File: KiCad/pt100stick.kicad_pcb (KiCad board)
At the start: 2 copper layers, 15.7 x 20.8 mm, 9 parts, among them U1 MAX31865ATP_

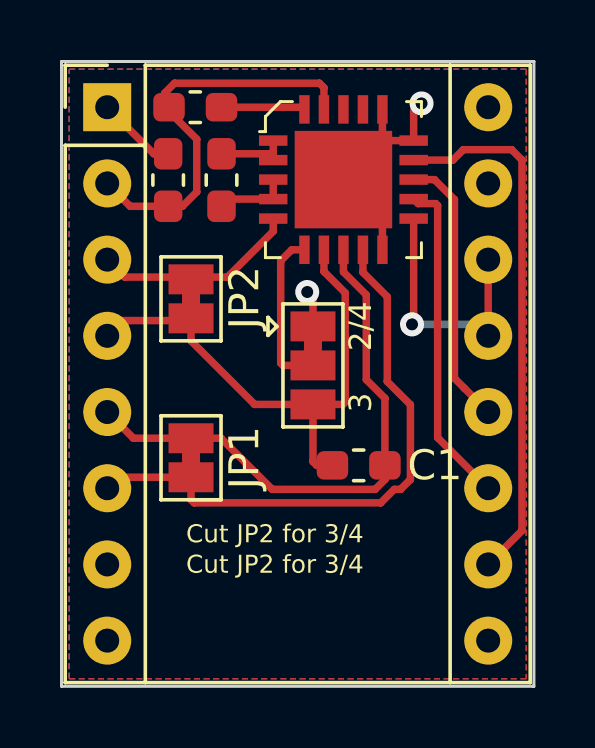
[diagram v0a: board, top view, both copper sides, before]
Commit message: Moved all footprints to project lib (I think)
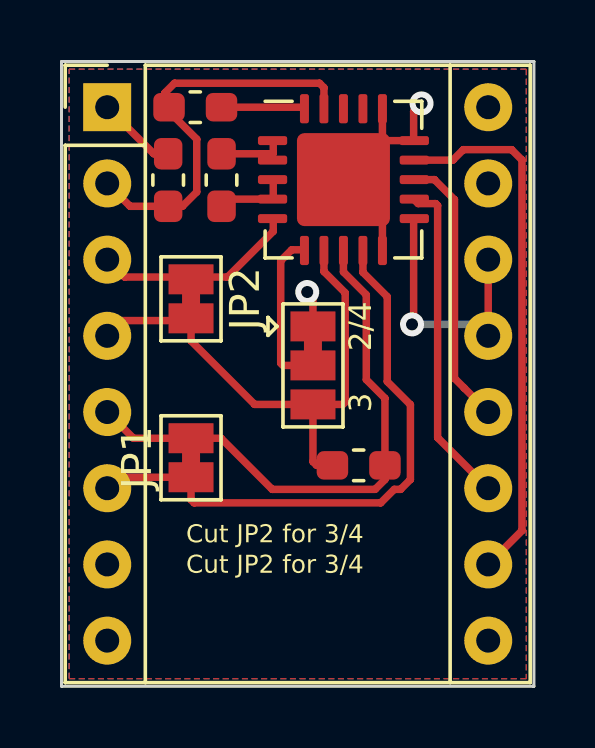
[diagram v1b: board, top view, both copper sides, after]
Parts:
- A1: footprint Module:Pololu_Breakout-16_15.2x20.3mm -> PT100Stick:Pololu_Breakout-16_15.2x20.3mm
- C1, C2: footprint Capacitor_SMD:C_0603_1608Metric_Pad1.05x0.95mm_HandSolder -> PT100Stick:C_0603_1608Metric_Pad1.05x0.95mm_HandSolder
- FB1: footprint Inductor_SMD:L_0603_1608Metric_Pad1.05x0.95mm_HandSolder -> PT100Stick:L_0603_1608Metric_Pad1.05x0.95mm_HandSolder
- JP1, JP2: footprint Jumper:SolderJumper-2_P1.3mm_Bridged_Pad1.0x1.5mm -> PT100Stick:SolderJumper-2_P1.3mm_Bridged_Pad1.0x1.5mm
- JP3: footprint Jumper:SolderJumper-3_P1.3mm_Bridged12_Pad1.0x1.5mm -> PT100Stick:SolderJumper-3_P1.3mm_Bridged12_Pad1.0x1.5mm
- R1: footprint Resistor_SMD:R_0603_1608Metric_Pad1.05x0.95mm_HandSolder -> PT100Stick:R_0603_1608Metric_Pad1.05x0.95mm_HandSolder
- U1: footprint digikey-footprints:TQFN-20-1EP_5x5mm -> PT100Stick:TQFN-20-1EP_5x5mm_P0.65mm_EP3.1x3.1mm

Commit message: Fix silkscreen issue
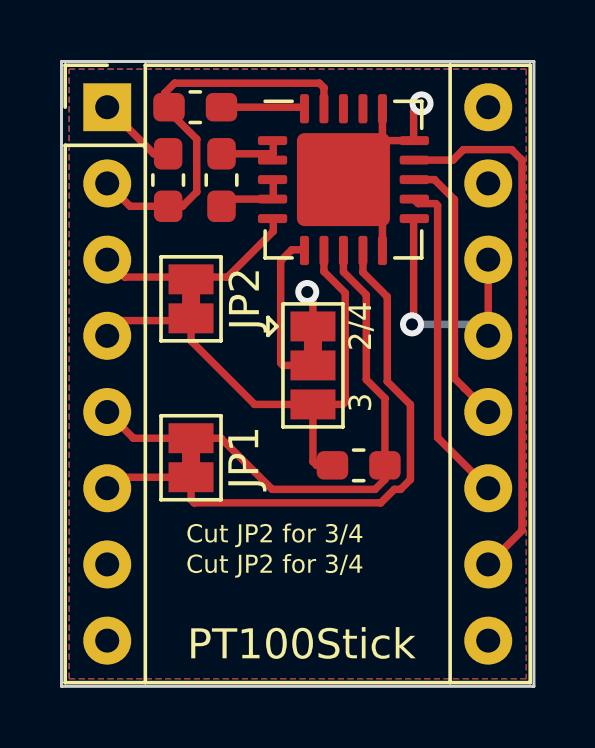
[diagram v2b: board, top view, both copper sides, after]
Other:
- board text added: "PT100Stick"
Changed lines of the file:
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@@
   (general
     (thickness 1.6)
-    (drawings 10)
+    (drawings 11)
     (tracks 105)
     (zones 0)
@@
     (tags "solder jumper open")
     (attr virtual)
-    (fp_text reference JP1 (at 0 -1.8 90) (layer F.SilkS)
+    (fp_text reference JP1 (at 0 1.778 90) (layer F.SilkS)
       (effects (font (size 1 1) (thickness 0.15)))
     )
@@
     )
   )
+  (gr_text PT100Stick (at 148.717 89.027) (layer F.SilkS)
+    (effects (font (size 1 1) (thickness 0.15)))
+  )
   (gr_text "Cut JP2 for 3/4" (at 147.828 86.36) (layer F.SilkS)

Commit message: Fix more silkscreen, gen gerbers
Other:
- board text added: "Cut JP1 for 4"
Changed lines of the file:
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@@
   (general
     (thickness 1.6)
-    (drawings 11)
+    (drawings 9)
     (tracks 105)
     (zones 0)
@@
       (outputformat 1)
       (mirror false)
-      (drillshape 1)
+      (drillshape 0)
       (scaleselection 1)
-      (outputdirectory ""))
+      (outputdirectory "Gerbers/"))
   )
   (net 0 "")
@@
     (effects (font (size 0.6 0.6) (thickness 0.15)))
   )
-  (gr_text "Cut JP2 for 3/4" (at 147.828 85.344) (layer F.SilkS)
+  (gr_text "Cut JP1 for 4" (at 147.828 85.344) (layer F.SilkS)
     (effects (font (size 0.6 0.6) (thickness 0.15)))
   )
@@
     (effects (font (size 0.75 0.75) (thickness 0.15)))
   )
-  (gr_text 2/4 (at 151.13 76.454 90) (layer B.SilkS)
-    (effects (font (size 1 1) (thickness 0.15)) (justify mirror))
-  )
-  (gr_text 3 (at 151.384 76.327 90) (layer B.SilkS)
-    (effects (font (size 1 1) (thickness 0.15)) (justify mirror))
-  )
   (gr_line (start 156.464 69.596) (end 156.464 90.424) (layer Edge.Cuts) (width 0.1))

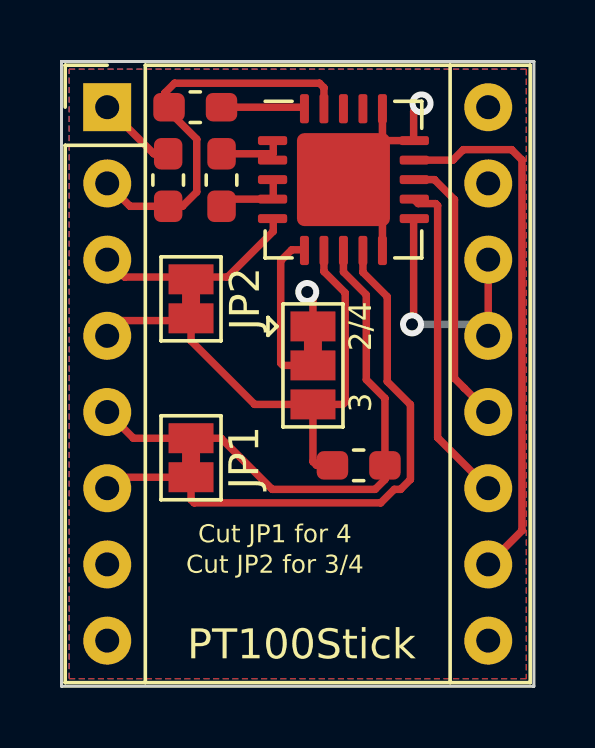
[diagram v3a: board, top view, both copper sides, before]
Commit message: Reworked layout
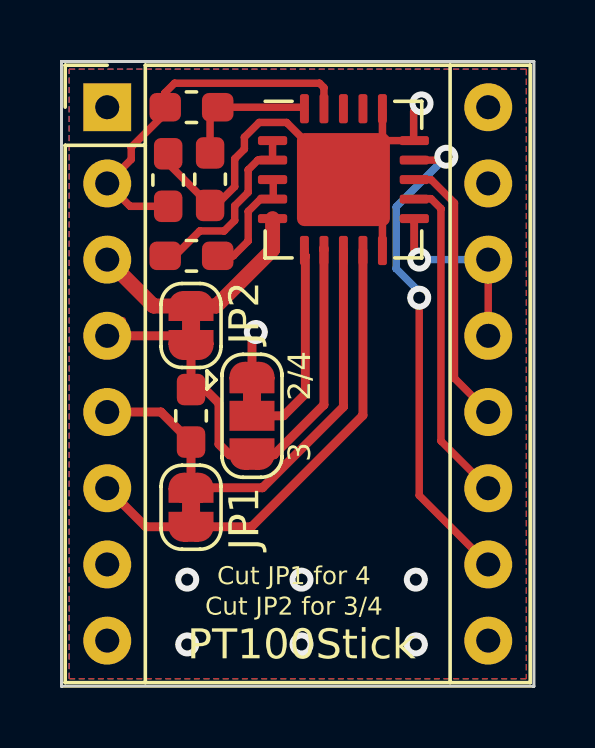
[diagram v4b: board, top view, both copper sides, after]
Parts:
- added C3: 0.1uF, PT100Stick:C_0603_1608Metric_Pad1.05x0.95mm_HandSolder, F.Cu at (145.7, 73.5)
- JP1, JP2: footprint PT100Stick:SolderJumper-2_P1.3mm_Bridged_Pad1.0x1.5mm -> PT100Stick:SolderJumper-2_P1.3mm_Bridged_RoundedPad1.0x1.5mm
- JP3: footprint PT100Stick:SolderJumper-3_P1.3mm_Bridged12_Pad1.0x1.5mm -> PT100Stick:SolderJumper-3_P1.3mm_Bridged12_RoundedPad1.0x1.5mm
- moved C1 5.83 mm to (145.0, 81.4), turned to 270 degrees
- moved R1 2.72 mm to (145.0, 76.1), turned to 180 degrees
- moved JP3 2.64 mm to (147.1, 81.4)
- moved JP1 1.65 mm to (145.0, 84.5)
- moved JP2 0.89 mm to (145.0, 78.4)
- moved FB1 0.13 mm to (145.0, 71.1)
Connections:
- net Net-(FB1-Pad2) renamed VDDA
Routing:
- net GND: track 12.0 -> 19.4 mm, vias 2 -> 8
- net /BIAS: track 2.67 -> 6.15 mm
- net /FORCE-: track 19.7 -> 16.6 mm
- net /RTDIN-: track 18.7 -> 16.1 mm
- net VDDA: track 2.94 -> 4.56 mm
- net /FORCE2: track 5.46 -> 6.88 mm
- net Net-(R1-Pad1): track 2.47 -> 3.84 mm
- net /MOSI: track 17.8 -> 16.7 mm, vias 0 -> 2
- net /FORCE+: track 6.83 -> 7.97 mm
- net +3V3: track 13.5 -> 12.4 mm
- net /MISO: track 8.79 -> 8.23 mm
- net /RTDIN+: track 17.8 -> 17.3 mm

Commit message: Commiting before final changes (need to swap miso and mosi)
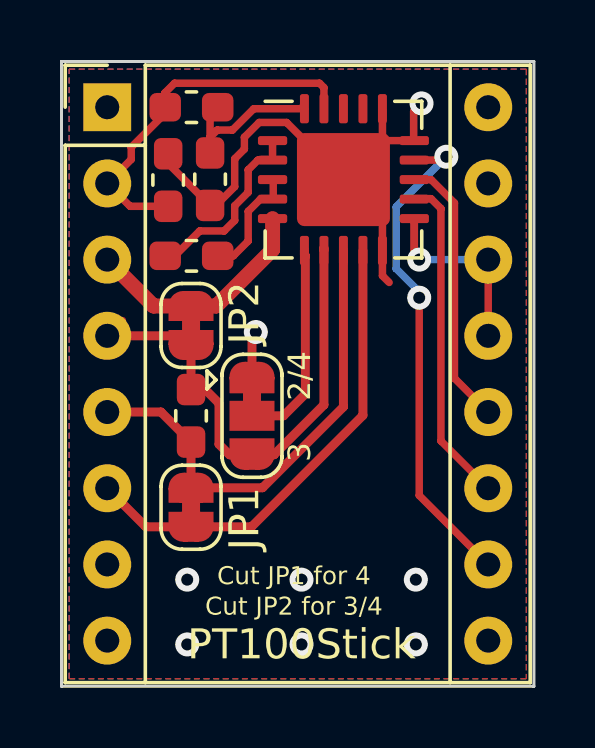
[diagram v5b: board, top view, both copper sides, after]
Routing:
- net VDDA: track 4.56 -> 5.80 mm
- net GND: track 19.4 -> 20.6 mm
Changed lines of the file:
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@@
     (thickness 1.6)
     (drawings 9)
-    (tracks 123)
+    (tracks 129)
     (zones 0)
     (modules 10)
@@
   )
   (setup
-    (last_trace_width 0.3)
+    (last_trace_width 0.25)
     (user_trace_width 0.3)
     (user_trace_width 0.4)
@@
   (via (at 152.527 89.027) (size 0.8) (drill 0.4) (layers F.Cu B.Cu) (net 5))
   (segment (start 144.145 72.87) (end 145.669 74.394) (width 0.25) (layer F.Cu) (net 5) (status 30))
+  (segment (start 151.414 75.8955) (end 151.414 76.738) (width 0.25) (layer F.Cu) (net 5))
+  (segment (start 151.414 76.738) (end 151.638 76.962) (width 0.25) (layer F.Cu) (net 5))
   (segment (start 154.94 78.74) (end 154.94 76.2) (width 0.25) (layer F.Cu) (net 6) (status 30))
   (segment (start 154.559 78.359) (end 154.94 78.74) (width 0.25) (layer B.Cu) (net 6) (status 30))
@@
   (segment (start 148.844 80.679) (end 148.116 81.407) (width 0.3) (layer F.Cu) (net 19))
   (segment (start 148.741 71.12) (end 148.814 71.193) (width 0.25) (layer F.Cu) (net 20) (status 30))
-  (segment (start 145.909 71.12) (end 148.741 71.12) (width 0.25) (layer F.Cu) (net 20) (status 30))
   (segment (start 145.669 71.374) (end 145.923 71.12) (width 0.25) (layer F.Cu) (net 20) (status 30))
   (segment (start 145.669 72.644) (end 145.669 71.374) (width 0.25) (layer F.Cu) (net 20) (status 30))
+  (segment (start 147.124388 71.1705) (end 148.814 71.1705) (width 0.25) (layer F.Cu) (net 20))
+  (segment (start 146.412888 71.882) (end 147.124388 71.1705) (width 0.25) (layer F.Cu) (net 20))
+  (segment (start 145.669 72.644) (end 145.669 72.119) (width 0.25) (layer F.Cu) (net 20))
+  (segment (start 145.906 71.882) (end 146.412888 71.882) (width 0.25) (layer F.Cu) (net 20))
+  (segment (start 145.669 72.119) (end 145.906 71.882) (width 0.25) (layer F.Cu) (net 20))
   (zone (net 5) (net_name GND) (layer B.Cu) (hatch edge 0.508)
     (connect_pads (clearance 0.508))

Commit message: Hopefully stable release :D
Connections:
- A1 pad 10: /MOSI -> /MISO
- A1 pad 13: /MISO -> /MOSI
- A1 pad 14: /MISO -> /MOSI
- A1 pad 15: Net-(A1-Pad15) -> (no net)
- A1 pad 16: Net-(A1-Pad16) -> (no net)
- A1 pad 8: Net-(A1-Pad8) -> (no net)
- A1 pad 9: Net-(A1-Pad9) -> (no net)
- U1 pad 17: Net-(U1-Pad17) -> (no net)
- U1 pad 18: Net-(U1-Pad18) -> (no net)
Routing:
- net /MOSI: track 16.7 -> 8.47 mm, vias 2 -> 1
- net /MISO: track 8.23 -> 12.5 mm, vias 1 -> 0
- net GND: track 20.6 -> 19.4 mm

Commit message: Quick fixes
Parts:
- moved C2 0.08 mm to (144.2, 73.5), turned to 270 degrees
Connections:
- A1 pad 1: GND -> (no net)
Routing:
- net GND: track 19.4 -> 17.1 mm, vias 8 -> 2
- net +3V3: track 12.4 -> 10.8 mm

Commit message: fix logo
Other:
- board text added: "This PCB design is licensed under GPL3"
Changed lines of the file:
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@@
   (general
     (thickness 1.6)
-    (drawings 31)
+    (drawings 32)
     (tracks 110)
     (zones 0)
@@
     (0 F.Cu signal)
     (31 B.Cu signal)
-    (32 B.Adhes user hide)
-    (33 F.Adhes user hide)
+    (32 B.Adhes user)
+    (33 F.Adhes user)
     (34 B.Paste user)
     (35 F.Paste user)
@@
     (38 B.Mask user)
     (39 F.Mask user)
-    (40 Dwgs.User user hide)
-    (41 Cmts.User user hide)
-    (42 Eco1.User user hide)
-    (43 Eco2.User user hide)
-    (44 Edge.Cuts user hide)
-    (45 Margin user hide)
-    (46 B.CrtYd user hide)
-    (47 F.CrtYd user hide)
-    (48 B.Fab user hide)
-    (49 F.Fab user hide)
+    (40 Dwgs.User user)
+    (41 Cmts.User user)
+    (42 Eco1.User user)
+    (43 Eco2.User user)
+    (44 Edge.Cuts user)
+    (45 Margin user)
+    (46 B.CrtYd user)
+    (47 F.CrtYd user)
+    (48 B.Fab user)
+    (49 F.Fab user)
   )
   (setup
@@
     )
   )
-  (gr_line (start 147.334001 83.81424) (end 147.334001 87.17464) (layer B.SilkS) (width 0.002))
-  (gr_line (start 150.244161 82.134001) (end 147.334001 83.81424) (layer B.SilkS) (width 0.002))
-  (gr_line (start 153.154241 87.17464) (end 153.154241 83.81424) (layer B.SilkS) (width 0.002))
-  (gr_line (start 151.099921 87.32112) (end 151.099921 87.32112) (layer B.SilkS) (width 0.002))
-  (gr_line (start 151.099921 87.32112) (end 150.222081 87.32112) (layer B.SilkS) (width 0.002))
-  (gr_line (start 148.604481 87.32112) (end 151.006161 83.6676) (layer B.SilkS) (width 0.002))
-  (gr_line (start 150.244161 82.134001) (end 150.244161 82.134001) (layer B.SilkS) (width 0.002))
-  (gr_line (start 153.154241 83.81424) (end 150.244161 82.134001) (layer B.SilkS) (width 0.002))
-  (gr_line (start 151.884001 83.6676) (end 149.482241 87.32112) (layer B.SilkS) (width 0.002))
-  (gr_line (start 148.604481 87.32112) (end 148.604481 87.32112) (layer B.SilkS) (width 0.002))
-  (gr_line (start 149.388401 83.6676) (end 149.388401 83.6676) (layer B.SilkS) (width 0.002))
-  (gr_line (start 152.300721 85.4944) (end 151.099921 87.32112) (layer B.SilkS) (width 0.002))
-  (gr_line (start 151.422721 85.4944) (end 152.300721 85.4944) (layer B.SilkS) (width 0.002))
-  (gr_line (start 147.334001 87.17464) (end 150.244161 88.85472) (layer B.SilkS) (width 0.002))
-  (gr_line (start 151.006161 83.6676) (end 151.884001 83.6676) (layer B.SilkS) (width 0.002))
-  (gr_line (start 150.222081 87.32112) (end 151.422721 85.4944) (layer B.SilkS) (width 0.002))
-  (gr_line (start 149.065521 85.4944) (end 148.187601 85.4944) (layer B.SilkS) (width 0.002))
-  (gr_line (start 149.388401 83.6676) (end 150.2664 83.6676) (layer B.SilkS) (width 0.002))
-  (gr_line (start 150.244161 88.85472) (end 153.154241 87.17464) (layer B.SilkS) (width 0.002))
-  (gr_line (start 149.482241 87.32112) (end 148.604481 87.32112) (layer B.SilkS) (width 0.002))
-  (gr_line (start 148.187601 85.4944) (end 149.388401 83.6676) (layer B.SilkS) (width 0.002))
-  (gr_line (start 150.2664 83.6676) (end 149.065521 85.4944) (layer B.SilkS) (width 0.002))
+  (gr_text "This PCB design is\nlicensed under GPL3" (at 145.0086 79.375 90) (layer B.SilkS)
+    (effects (font (size 0.75 0.75) (thickness 0.15)) (justify mirror))
+  )
+  (gr_line (start 147.76312 81.218699) (end 146.50306 79.036079) (layer B.SilkS) (width 0.075))
+  (gr_line (start 150.28342 81.218699) (end 147.76312 81.218699) (layer B.SilkS) (width 0.075))
+  (gr_line (start 150.28342 76.853519) (end 151.543599 79.036079) (layer B.SilkS) (width 0.075))
+  (gr_line (start 146.50306 79.036079) (end 147.76312 76.853519) (layer B.SilkS) (width 0.075))
+  (gr_line (start 151.543599 79.036079) (end 150.28342 81.218699) (layer B.SilkS) (width 0.075))
+  (gr_line (start 150.3934 79.677899) (end 150.3934 79.0194) (layer B.SilkS) (width 0.075))
+  (gr_line (start 151.543599 79.036079) (end 151.543599 79.036079) (layer B.SilkS) (width 0.075))
+  (gr_line (start 147.76312 76.853519) (end 150.28342 76.853519) (layer B.SilkS) (width 0.075))
+  (gr_line (start 147.65326 79.052639) (end 149.0233 78.152159) (layer B.SilkS) (width 0.075))
+  (gr_line (start 147.65326 79.607519) (end 147.65326 80.265839) (layer B.SilkS) (width 0.075))
+  (gr_line (start 150.3934 77.806199) (end 147.65326 79.607519) (layer B.SilkS) (width 0.075))
+  (gr_line (start 147.65326 78.394259) (end 147.65326 78.394259) (layer B.SilkS) (width 0.075))
+  (gr_line (start 147.65326 78.394259) (end 147.65326 79.052639) (layer B.SilkS) (width 0.075))
+  (gr_line (start 150.3934 78.464579) (end 150.3934 77.806199) (layer B.SilkS) (width 0.075))
+  (gr_line (start 149.0233 77.493659) (end 147.65326 78.394259) (layer B.SilkS) (width 0.075))
+  (gr_line (start 147.65326 80.265839) (end 150.3934 78.464579) (layer B.SilkS) (width 0.075))
+  (gr_line (start 149.0233 78.152159) (end 149.0233 77.493659) (layer B.SilkS) (width 0.075))
+  (gr_line (start 147.65326 80.265839) (end 147.65326 80.265839) (layer B.SilkS) (width 0.075))
+  (gr_line (start 149.0233 80.578499) (end 150.3934 79.677899) (layer B.SilkS) (width 0.075))
+  (gr_line (start 150.3934 79.677899) (end 150.3934 79.677899) (layer B.SilkS) (width 0.075))
+  (gr_line (start 149.0233 79.920059) (end 149.0233 80.578499) (layer B.SilkS) (width 0.075))
+  (gr_line (start 150.3934 79.0194) (end 149.0233 79.920059) (layer B.SilkS) (width 0.075))
   (gr_text PT100Stick (at 148.717 89.027) (layer F.SilkS)
     (effects (font (size 1 1) (thickness 0.15)))
@@
       )
     )
-  )
-  (zone (net 0) (net_name "") (layer F.Cu) (hatch edge 0.508)
-    (connect_pads (clearance 0.508))
-    (min_thickness 0.254)
-    (keepout (tracks allowed) (vias allowed) (copperpour not_allowed))
-    (fill (arc_segments 32) (thermal_gap 0.508) (thermal_bridge_width 0.508))
-    (polygon
-      (pts
-        (xy 152.9842 82.0928) (xy 150.1902 82.169) (xy 150.3172 76.708) (xy 153.035 76.6826)
-      )
-    )
